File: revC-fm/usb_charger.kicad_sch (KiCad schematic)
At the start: 15 parts, among them U11 BQ25883RGER

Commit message: updated fab files
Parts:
- C33: Manufacturer (none) -> TDK; Mfr. Part No (none) -> CGA3E1X7R1V105K080AE
- C34, C38: Manufacturer (none) -> TDK
- C35, C36: Manufacturer (none) -> Murata
- C39: Manufacturer (none) -> TDK; Mfr. Part No (none) -> CGA2B3X7R1H473K050BB
- C40: Manufacturer (none) -> Murata; Mfr. Part No (none) -> GRT188R61C475KE13J
- L2: Manufacturer (none) -> Würth Elektronik
- R31, R36: Manufacturer (none) -> Stackpole Electronics; Mfr. Part No (none) -> RMCF0402FT10K0
- R32: Manufacturer (none) -> Stackpole Electronics; Mfr. Part No (none) -> RMCF0402FT100K
- R34: Manufacturer (none) -> Stackpole Electronics; Mfr. Part No (none) -> RMCF0603FT5K23
- R35: Manufacturer (none) -> Stackpole Electronics; Mfr. Part No (none) -> RMCF0603FG30K1
- R37: Manufacturer (none) -> Stackpole Electronics; Mfr. Part No (none) -> RMCF0603FT3K16
- U11: Manufacturer (none) -> Texas Instruments

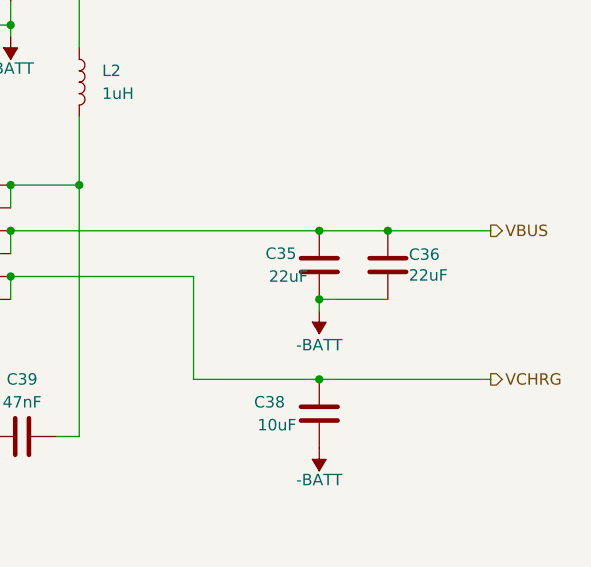
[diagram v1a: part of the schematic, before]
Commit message: updated per review, improved docs
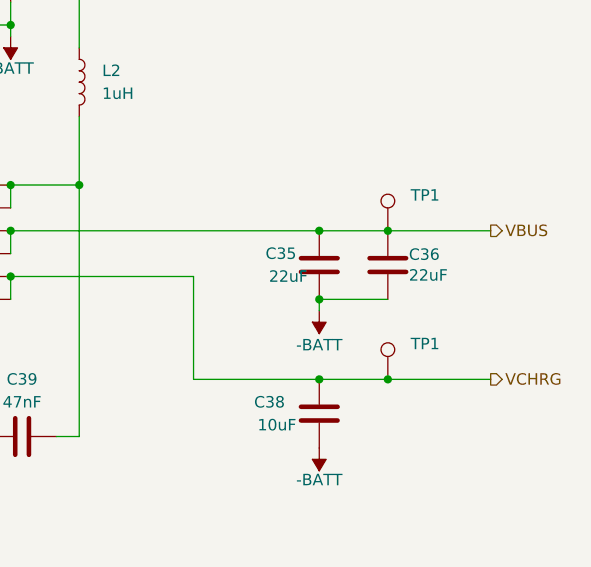
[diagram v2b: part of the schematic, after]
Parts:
- added TP1 (x2): RCU-0C, SierraLobo:TestPoint_TE_RCU_0603, symbol Connector:TestPoint
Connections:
- net VBUS: now also TP1.1
- net VCHRG: now also TP1.1
